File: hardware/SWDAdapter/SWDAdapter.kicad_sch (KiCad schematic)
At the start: 5 parts, among them J1 Conn_ARM_JTAG_SWD_10, J2 Conn_01x03_Female, J3 ST-Link_IDC, J4 Conn_02x03_Odd_Even, J5 Conn_01x05_Male

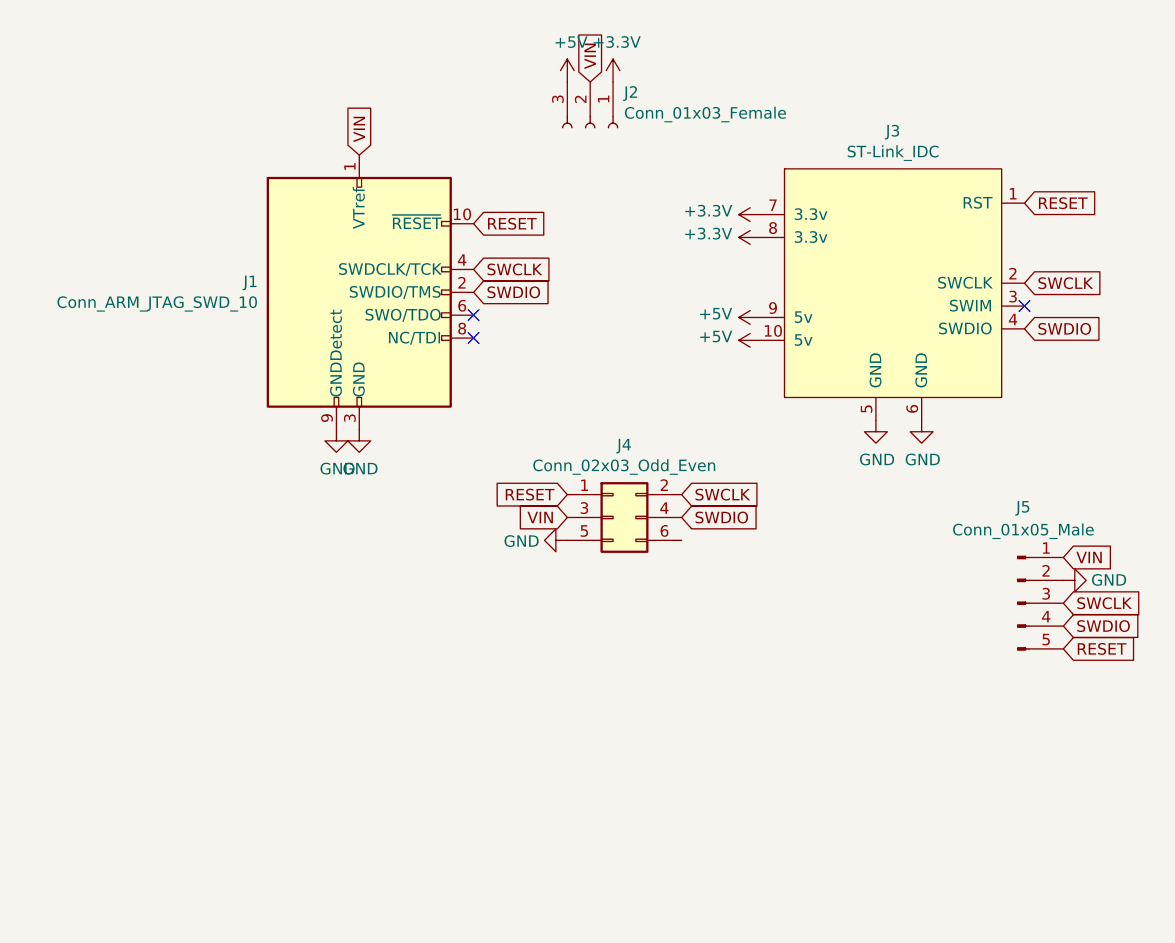
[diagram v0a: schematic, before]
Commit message: adjustments to SWD adapter PCB to support 14pin STM32 connector
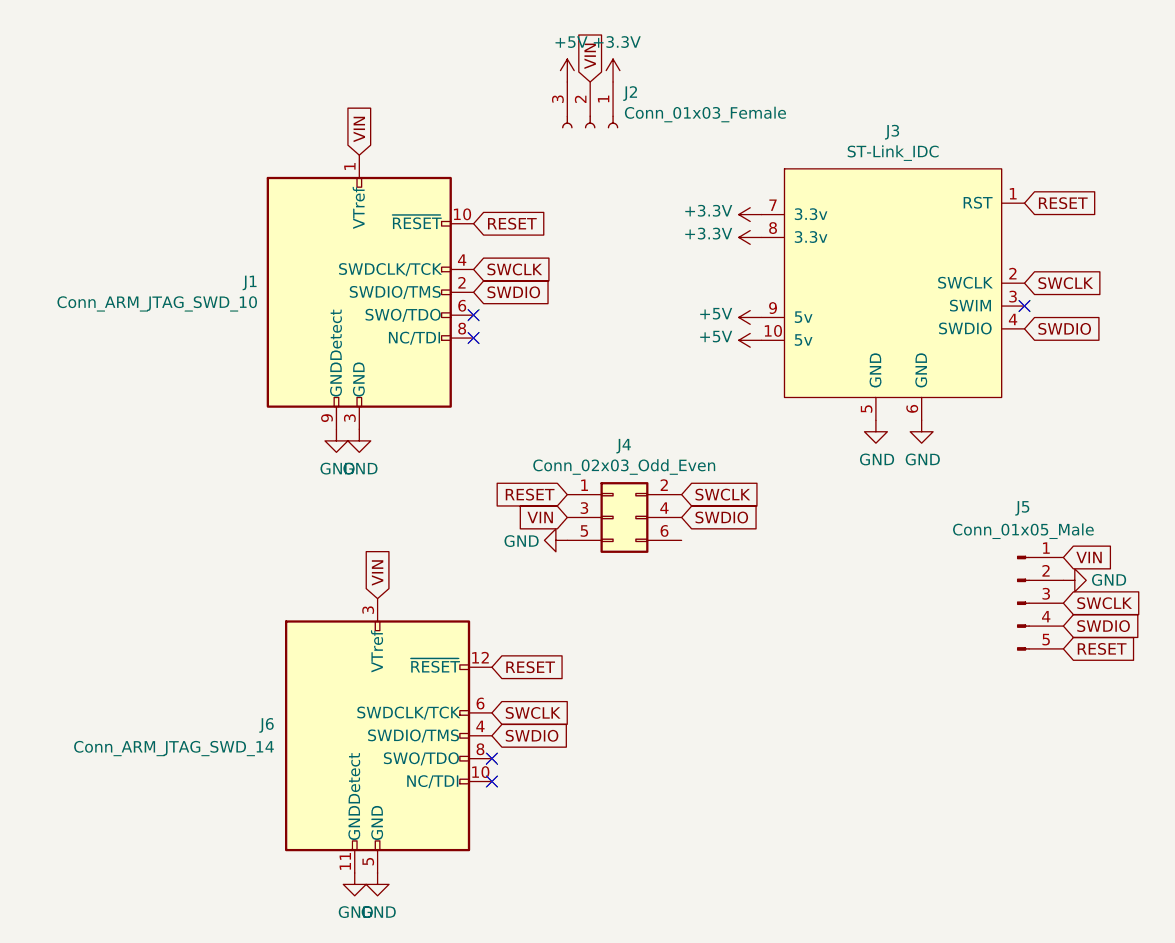
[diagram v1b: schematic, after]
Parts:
- added J6: Conn_ARM_JTAG_SWD_14, UsefulModifications:SWD14 STLINK-V3-Mini, symbol STDC14-V3Mini-JTAG:Conn_ARM_JTAG_SWD_14
- J1: footprint UsefulModifications:JTAG_SWD_SMD -> UsefulModifications:CONN_3220-10-0100-00_CNC
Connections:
- net GND: now also J6.11 (GNDDetect), J6.5 (GND), J6.7 (KEY)
- net RESET: now also J6.12 (~{RESET})
- net SWCLK: now also J6.6 (SWDCLK/TCK)
- net SWDIO: now also J6.4 (SWDIO/TMS)
- net VIN: now also J6.3 (VTref)
- new net Reserved: J6.1 (Reserved), J6.13 (Reserved), J6.14 (Reserved), J6.2 (Reserved)
- no-connect marks 3 -> 5
